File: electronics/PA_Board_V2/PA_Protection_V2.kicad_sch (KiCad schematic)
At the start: 60 parts, among them J1 USB_B_Micro, J10 Conn_01x04, J2 Conn_01x05, J3 Conn_01x05, J4 Conn_01x04, Q3 2N7002, SW1 SW_Push, U1 ATSAMD21E18A-A, U12 74LV1T34, U2 LM75B, U3 LM2904

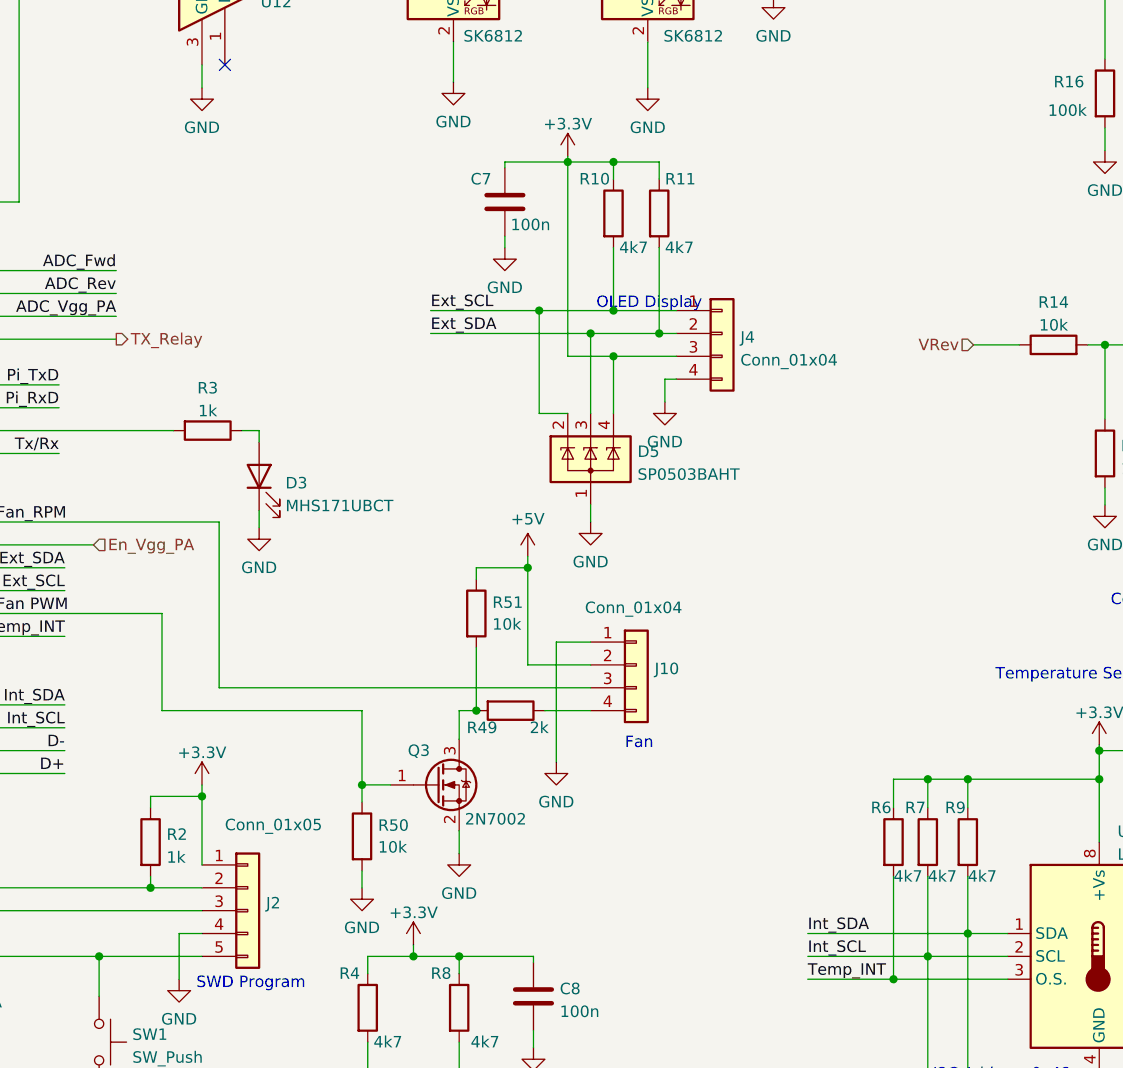
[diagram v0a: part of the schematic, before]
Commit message: Add RF Screen and some PCB and BOM changes
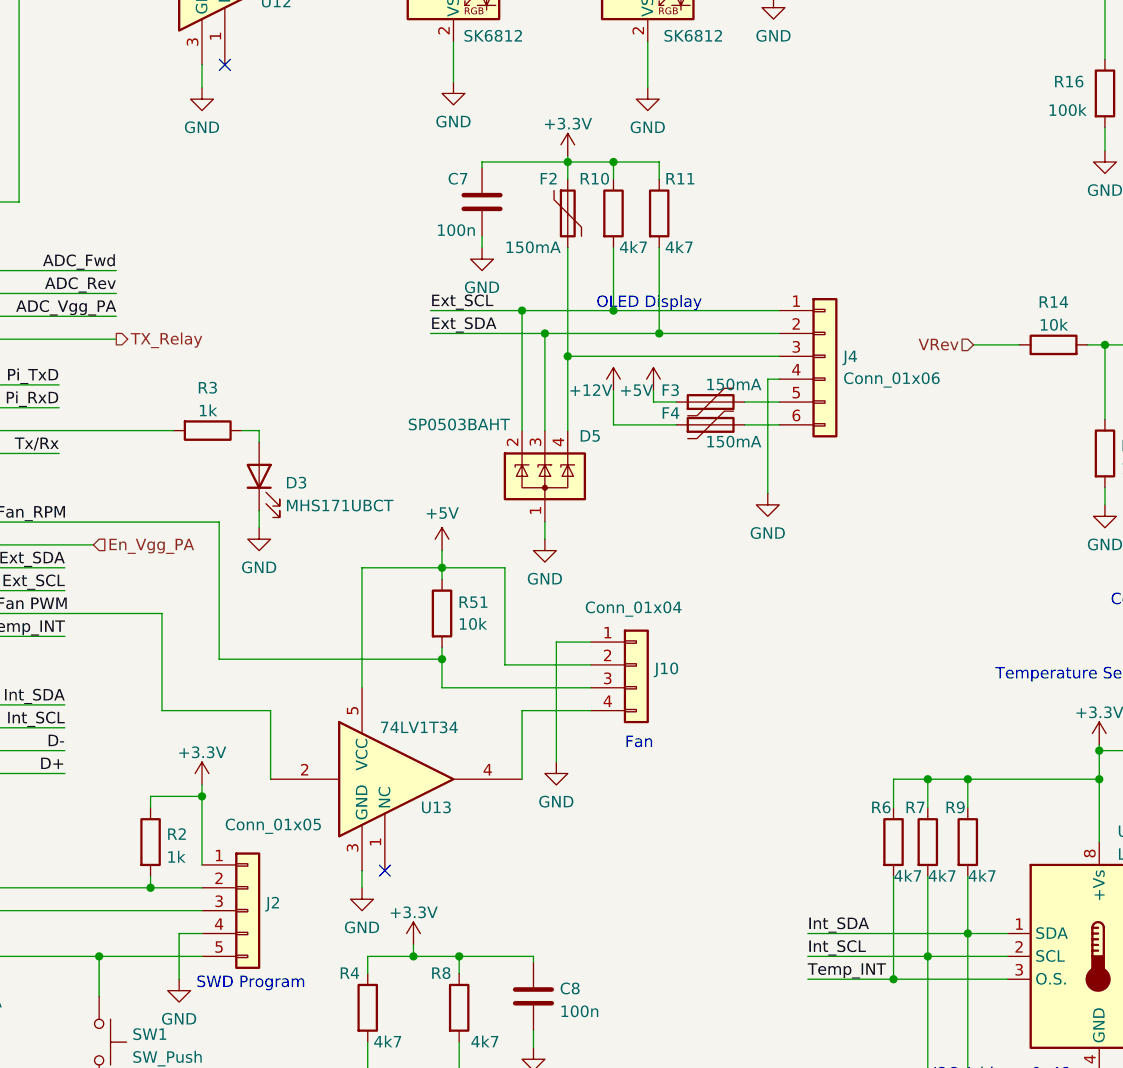
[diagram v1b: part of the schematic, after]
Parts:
- removed J4: Conn_01x04, Pi_Tx_V2:JST_PH_S4B-PH-SM4-TB_1x04-1MP_P2.00mm_Horizontal, symbol Connector_Generic:Conn_01x04
- removed Q3: 2N7002, Package_TO_SOT_SMD:SOT-23, symbol Transistor_FET:2N7002
- removed R49: 2k, Resistor_SMD:R_0603_1608Metric, symbol Device:R
- removed R50: 10k, Resistor_SMD:R_0603_1608Metric, symbol Device:R
- added F2, F3, F4: 150mA, Fuse:Fuse_0805_2012Metric, symbol Device:Polyfuse
- added J4: Conn_01x06, Pi_Tx_V2:JST_PH_S6B-PH-SM4-TB_1x06-1MP_P2.00mm_Horizontal, symbol Connector_Generic:Conn_01x06
- added U13: 74LV1T34, Package_TO_SOT_SMD:SOT-353_SC-70-5, symbol 74xGxx:74LVC1G34
- D1, D4, D5: LCSC Part C7074 -> C2682275
- J3: LCSC Part C7429691 -> C7429692
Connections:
- net +3.3V: now also F2.1; no longer D5.4 (K)
- net +5V: now also F3.1, U13.5 (VCC)
- net Ext_SCL: now also J4.1 (Pin_1)
- net Ext_SDA: now also J4.2 (Pin_2)
- net Fan PWM: now also U13.2
- net Fan_RPM: now also R51.2
- net GND: now also J4.4 (Pin_4), U13.3 (GND)
- net at J10.4 (Pin_4): now also U13.4
- new net: F3.2, J4.5 (Pin_5)
- new net: D5.4 (K), F2.2, J4.3 (Pin_3)
- new net: F4.2, J4.6 (Pin_6)
- new net +12V: F4.1
- no-connect marks 8 -> 9
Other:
- moved on the sheet: C7, D5, R51

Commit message: Latest version
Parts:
- renumbered C9 to C2, C8 to C24, C1 to C37, C7 to C39, C4 to C40, C11 to C43, C6 to C44, C3 to C45, C10 to C48, C12 to C50, C55 to C52, C2 to C53, C5 to C54, D4 to D1, D6 to D10, D3 to D13, D19 to D14, D18 to D15, D7 to D6, D1 to D8, J2 to J10, J10 to J2, J4 to J6, J1 to J9, L1 to L9, R9 to R1, R51 to R11, R4 to R16, R8 to R18, R15 to R19, R12 to R21, R10 to R24, R11 to R25, R24 to R26, R13 to R27, R20 to R28, R16 to R29, R23 to R30, R18 to R31, R17 to R32, R14 to R33, R19 to R34, R21 to R35, R25 to R36, R22 to R37, R3 to R42, R1 to R43, R2 to R44, R7 to R5, U3 to U12, U1 to U13, U12 to U15, U13 to U5
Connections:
- net DRIVER_EN: now reaches U13.8 (PA07)
- no-connect marks 9 -> 8
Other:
- note added: "Arduino Pin Mapping ATSAMD21E18 I/O Multiplexer 0 PA00 SK6812 DATA 1 PA03 ADC_FWD 2 PA04 ADC_REV 3 PA05 ADC_VGG 4 PA06 TX_RELAY 5 PA07 DRIVER_EN 6 PA08 SERCOM0 PAD 0 PI_TXD 7 PA09 SERCOM0 PAD 1 PI_RXD 8 PA10 WATCHDOG_LED 9 PA11 PI_TXEN 10 PA14 FAN_RPM 11 PA15 EN_VGG 12 PA16 SERCOM1 PAD 0 EXT_SDA 13 PA17 SERCOM1 PAD 1 EXT_SCL 14 PA18 FAN_PWM 15 PA19 LM75_INT 16 PA22 SERCOM3 PAD 0 INT_SDA 17 PA23 S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"
- note removed: "Arduino Pin Mapping ATSAMD21E18 I/O Multiplexer 0 PA00 DOTSTAR SDI 1 PA01 DOTSTAR CLK 2 PA03 ADC_FWD 3 PA04 ADC_REV 4 PA05 ADC_Vgg 5 PA06 TX_Relay_Out 6 PA08 SERCOM0 PAD 0 Slave_TxD 7 PA09 SERCOM0 PAD 1 Slave_RxD 8 PA10 Watchdog LED 9 PA11 SLAVE GPIO INT 10 PA15 En_Vgg_PA 11 PA16 SERCOM1 PAD 0 Ext_SDA 12 PA17 SERCOM1 PAD 1 Ext_SCL 13 PA19 LM75 Interrupt 14 PA22 SERCOM3 PAD 0 Int_SDA 15 PA23 SERCO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"
